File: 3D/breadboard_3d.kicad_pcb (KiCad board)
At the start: 2 copper layers, 171.1 x 126.6 mm, 1 part

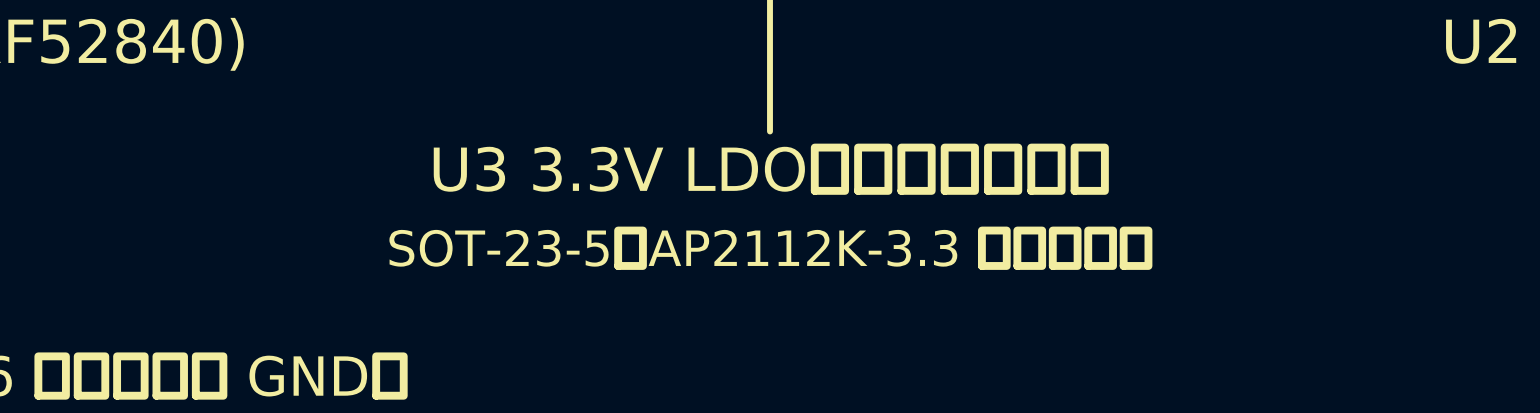
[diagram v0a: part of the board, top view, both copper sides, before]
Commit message: Correct wiring from annotated photos and identify U3 as DMC2038LVT
- Green GND wire lands on column 28 lower; add 27-top to 29-bottom link
- Fix long yellow P0.06 wire that never rendered (tube frame collapse)
- Purple wire no longer hidden under the red one
- Relabel U3 as DMC2038LVT complementary MOSFET in all figures and README

Co-Authored-By: Claude Opus 5.5 <noreply@anthropic.com>
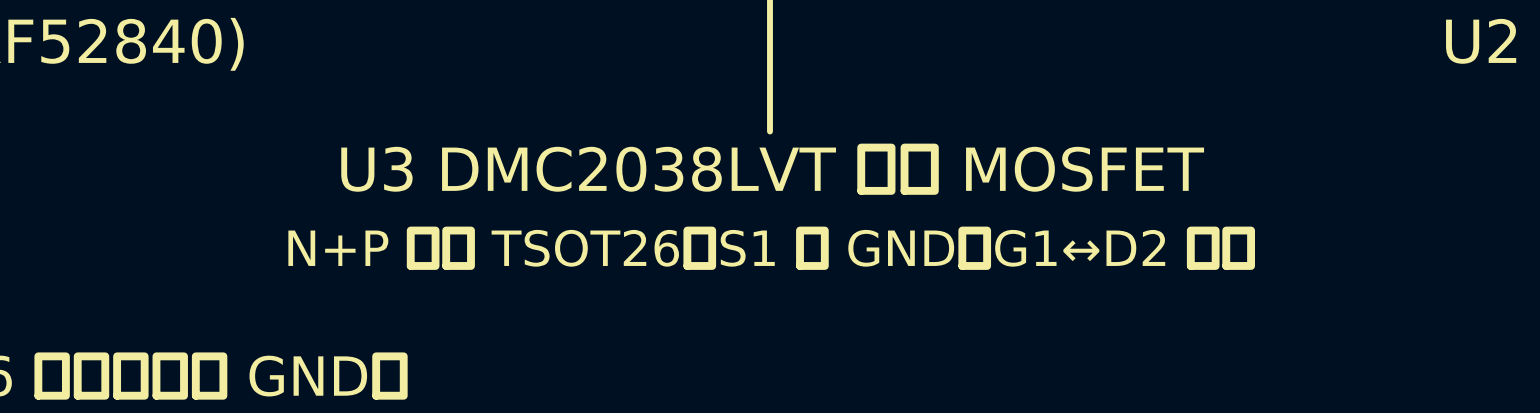
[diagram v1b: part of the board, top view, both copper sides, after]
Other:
- board text added: "N+P 通道 TSOT26；S1 接 GND、G1↔D2 相連"
- board text added: "U3 DMC2038LVT 互補 MOSFET"
- board text removed: "SOT-23-5，AP2112K-3.3 同腳位系列"
- board text removed: "U3 3.3V LDO（依接法推斷）"
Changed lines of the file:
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@@
 (gr_text "U1 nice!nano 相容 (nRF52840)" (at 69.26 134.00 0) (layer "F.SilkS") (effects (font (size 2.2 2.2) (thickness 0.4)) (justify left)))
 (gr_line (start 85.23 128.30) (end 85.23 132.00) (stroke (width 0.3) (type default)) (layer "F.SilkS"))
-(gr_text "U3 3.3V LDO（依接法推斷）" (at 139.84 140.50 0) (layer "F.SilkS") (effects (font (size 2.2 2.2) (thickness 0.4))))
-(gr_text "SOT-23-5，AP2112K-3.3 同腳位系列" (at 139.84 144.50 0) (layer "F.SilkS") (effects (font (size 1.8 1.8) (thickness 0.4))))
+(gr_text "U3 DMC2038LVT 互補 MOSFET" (at 139.84 140.50 0) (layer "F.SilkS") (effects (font (size 2.2 2.2) (thickness 0.4))))
+(gr_text "N+P 通道 TSOT26；S1 接 GND、G1↔D2 相連" (at 139.84 144.50 0) (layer "F.SilkS") (effects (font (size 1.8 1.8) (thickness 0.4))))
 (gr_line (start 139.84 128.30) (end 139.84 138.50) (stroke (width 0.3) (type default)) (layer "F.SilkS"))
 (gr_text "U2 WeAct BlackPill (STM32F401/F411)" (at 231.74 134.00 0) (layer "F.SilkS") (effects (font (size 2.2 2.2) (thickness 0.4)) (justify right)))
